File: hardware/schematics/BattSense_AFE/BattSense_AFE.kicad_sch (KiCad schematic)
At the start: 6 parts, among them J1 Battery, J2 ESP32_ADC

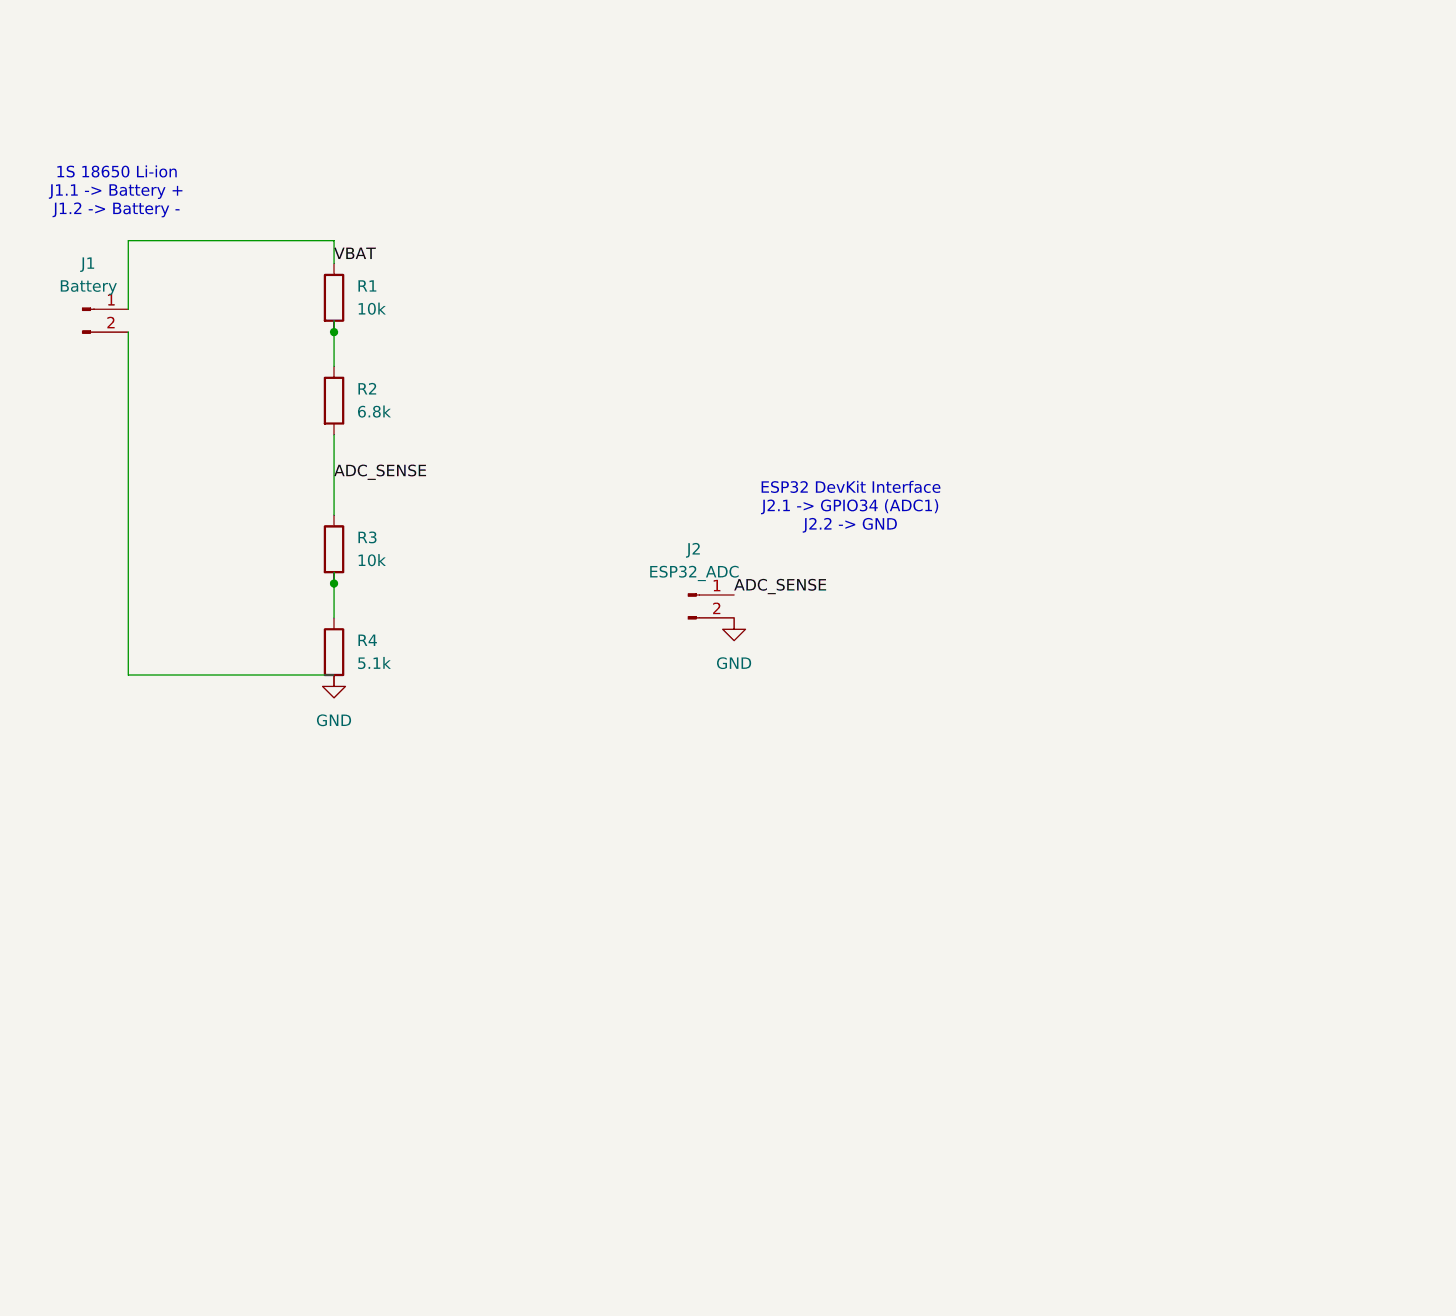
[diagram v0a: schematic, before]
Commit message: Complete BattSense Rev A hardware and documentation
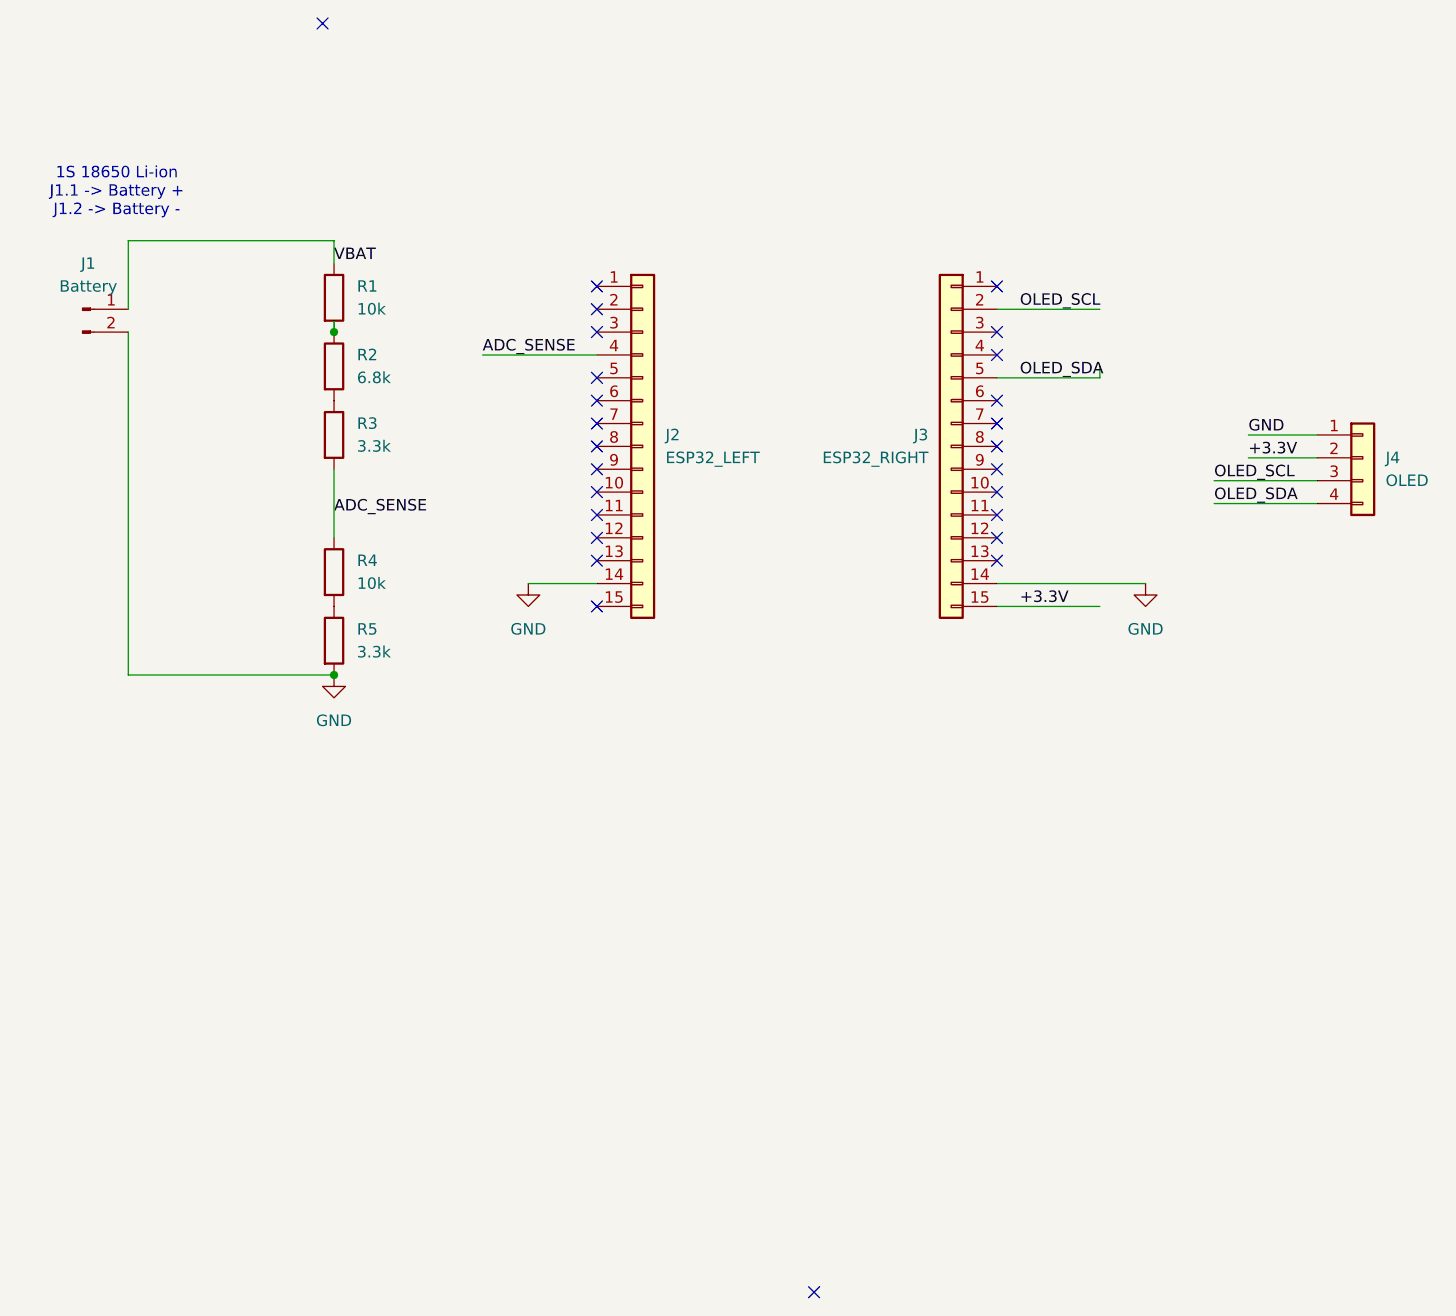
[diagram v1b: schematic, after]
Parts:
- removed J2: ESP32_ADC, Inductor_THT:L_CommonMode_PulseElectronics_PH9455x105NL_1, symbol Connector:Conn_01x02_Pin
- removed R4: 5.1k, symbol Device:R
- added J2: ESP32_LEFT, Connector_PinSocket_2.54mm:PinSocket_1x15_P2.54mm_Vertical, symbol Connector_Generic:Conn_01x15
- added J3: ESP32_RIGHT, Connector_PinSocket_2.54mm:PinSocket_1x15_P2.54mm_Vertical, symbol Connector_Generic:Conn_01x15
- added J4: OLED, Connector_PinHeader_2.54mm:PinHeader_1x04_P2.54mm_Vertical, symbol Connector_Generic:Conn_01x04
- added R3, R5: 3.3k, Resistor_THT:R_Axial_DIN0207_L6.3mm_D2.5mm_P10.16mm_Horizontal, symbol Device:R
- J1: footprint (none) -> Connector_PinHeader_2.54mm:PinHeader_1x02_P2.54mm_Vertical
- R1, R2: footprint (none) -> Resistor_THT:R_Axial_DIN0207_L6.3mm_D2.5mm_P10.16mm_Horizontal
- R4: renamed from R3; footprint (none) -> Resistor_THT:R_Axial_DIN0207_L6.3mm_D2.5mm_P10.16mm_Horizontal
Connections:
- net ADC_SENSE: now also J2.4 (Pin_4), R3.2; no longer R2.2
- net GND: now also J2.14 (Pin_14), J3.14 (Pin_14), J4.1 (Pin_1), R5.2
- net at R4.2: now also R5.1
- new net: R2.2, R3.1
- new net +3.3V: J3.15 (Pin_15), J4.2 (Pin_2)
- new net OLED_SCL: J3.2 (Pin_2), J4.3 (Pin_3)
- new net OLED_SDA: J3.5 (Pin_5), J4.4 (Pin_4)
- no-connect marks 0 -> 26
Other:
- note removed: "ESP32 DevKit Interface J2.1 -> GPIO34 (ADC1) J2.2 -> GND"
- moved on the sheet: R2, R4
